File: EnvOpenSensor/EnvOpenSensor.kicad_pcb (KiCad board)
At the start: 2 copper layers, 89.7 x 67.5 mm, 31 parts, among them J1 USB_C_Receptacle_USB2.0_16P, J2 AVR-ISP-6, SW1 SW_Push, SW2 SW_Push, SW3 SW_Push, SW4 SW_Push, U1 SCD41-D-R2, U2 Si7021-A20, U3 SPX3819M5-L-3-3, U4 ATtiny85-20S

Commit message: forgot some stuff
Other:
- board text added: "EnvOpenSensor"
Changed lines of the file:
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@@
   )
   (footprint "Button_Switch_Keyboard:SW_Cherry_MX_1.00u_PCB" (layer "F.Cu")
-    (at 71.94 36.12)
+    (at 71.94 36.11)
     (descr "Cherry MX keyswitch, 1.00u, PCB mount, http://cherryamericas.com/wp-content/uploads/2014/12/mx_cat.pdf")
     (tags "Cherry MX keyswitch 1.00u PCB")
@@
   )
   (footprint "Button_Switch_Keyboard:SW_Cherry_MX_1.00u_PCB" (layer "F.Cu")
-    (at 33.44 36.12)
+    (at 33.39 36.12)
     (descr "Cherry MX keyswitch, 1.00u, PCB mount, http://cherryamericas.com/wp-content/uploads/2014/12/mx_cat.pdf")
     (tags "Cherry MX keyswitch 1.00u PCB")
@@
   )
   (footprint "Button_Switch_Keyboard:SW_Cherry_MX_1.00u_PCB" (layer "F.Cu")
-    (at 52.69 36.12)
+    (at 52.64 36.12)
     (descr "Cherry MX keyswitch, 1.00u, PCB mount, http://cherryamericas.com/wp-content/uploads/2014/12/mx_cat.pdf")
     (tags "Cherry MX keyswitch 1.00u PCB")
@@
   (gr_line (start 15 77.5) (end 15 15)
     (stroke (width 0.1) (type default)) (layer "Edge.Cuts"))
+  (gr_text "EnvOpenSensor" (at 59.75 31.9) (layer "F.Cu")
+    (effects (font (size 0.8 0.8) (thickness 0.15) bold))
+  )
   (gr_text "env" (at 59.825 70) (layer "F.Mask")
     (effects (font (face "Dissolve Regular") (size 5 5) (thickness 0.15)))

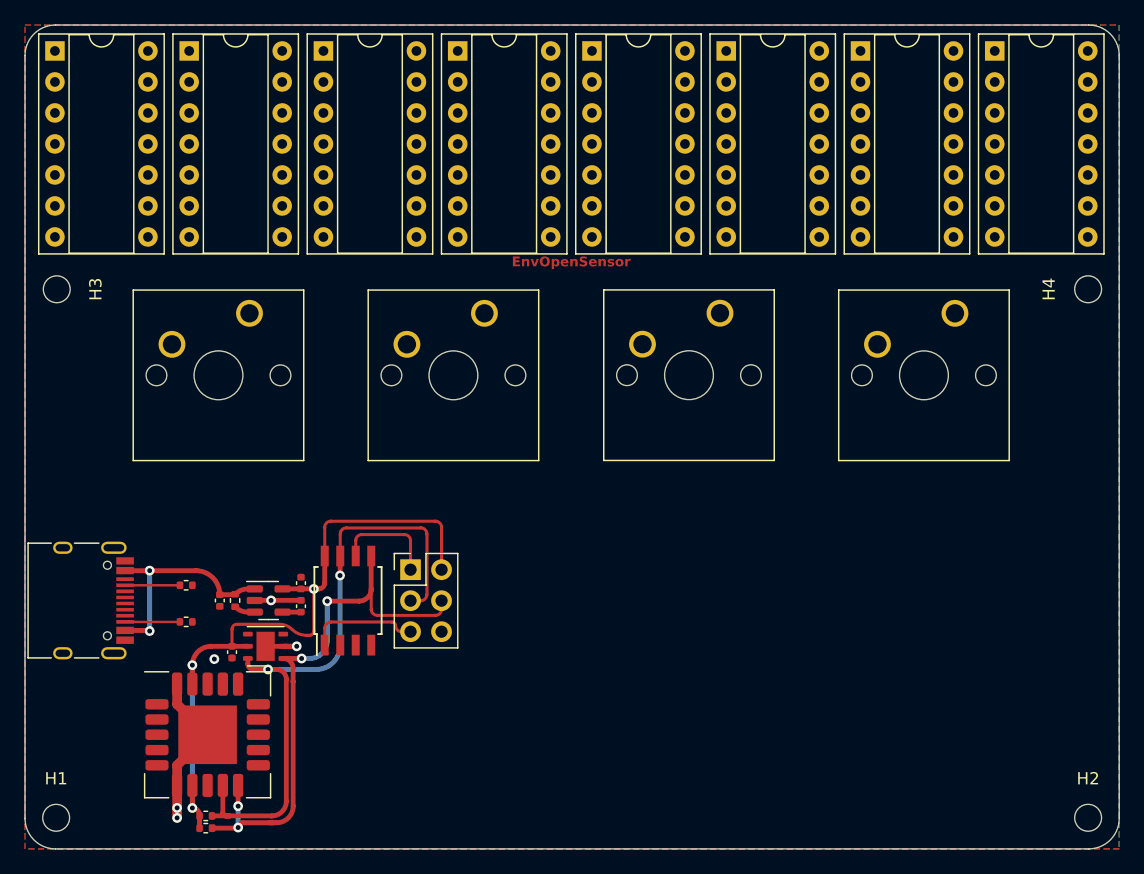
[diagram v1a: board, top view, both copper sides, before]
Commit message: added 3d models and shuffled some parts about for better usability.
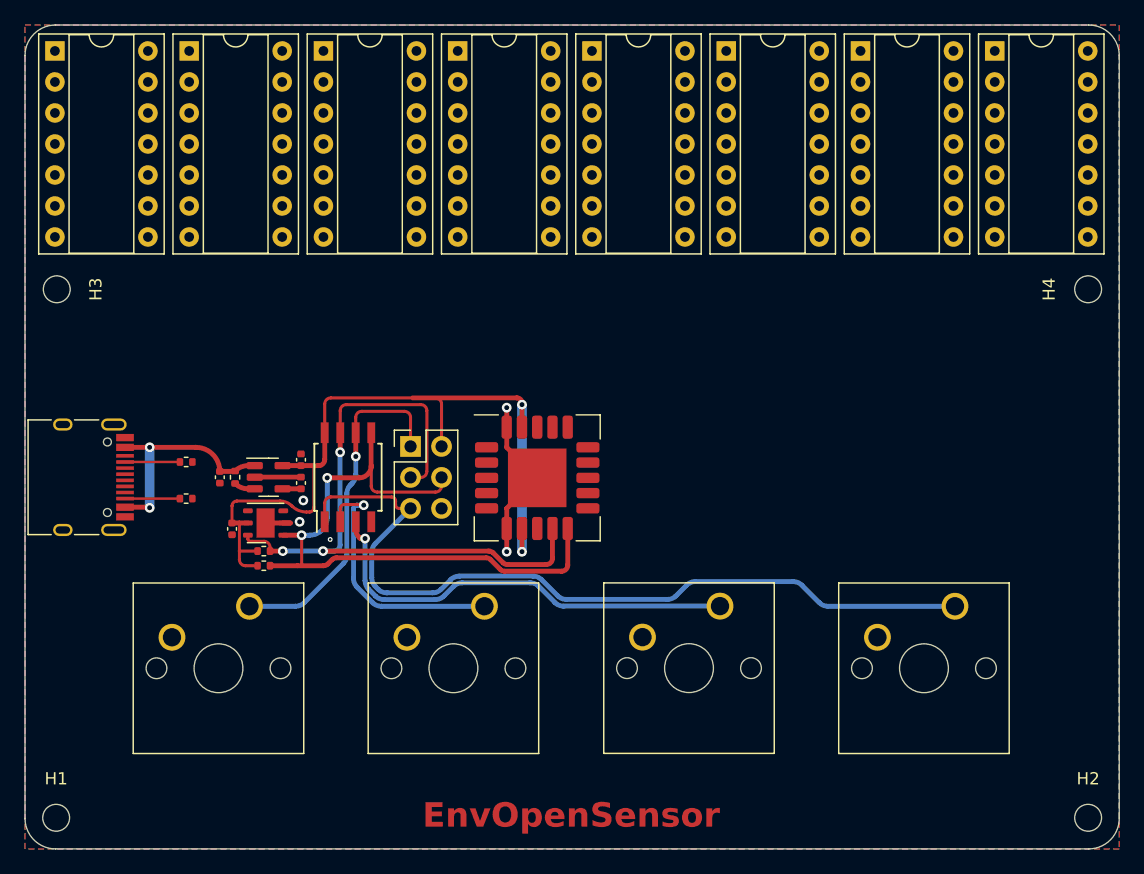
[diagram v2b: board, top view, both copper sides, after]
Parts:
- moved U1 34.2 mm to (57.0, 49.6)
- moved SW1 24.0 mm to (33.4, 60.1)
- moved SW2 24.0 mm to (52.6, 60.1)
- moved SW3 24.0 mm to (71.9, 60.1)
- moved SW4 24.0 mm to (91.2, 60.1)
- moved R5 22.2 mm to (34.6, 55.6)
- moved R4 22.0 mm to (34.6, 56.8)
- moved C2 10.1 mm to (31.0, 49.5)
- moved C3 10.1 mm to (37.6, 48.1)
- moved C4 10.1 mm to (32.0, 53.8)
- moved J1 10.1 mm to (19.1, 49.5)
- moved J2 10.1 mm to (46.6, 47.0)
- moved R1 10.1 mm to (28.2, 48.3)
- moved R2 10.1 mm to (28.2, 51.3)
- moved R3 10.1 mm to (32.2, 49.5)
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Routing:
- net PB5: track 9.10 -> 67.3 mm
- net PB4: track 0.00 -> 36.4 mm, vias 0 -> 1
- net PB3: track 0.00 -> 22.3 mm, vias 0 -> 1
- net PB1: track 8.65 -> 28.7 mm, vias 0 -> 1
- net +3V3: track 56.5 -> 66.7 mm, vias 3 -> 2
- net PB0: track 49.8 -> 57.1 mm, vias 4 -> 2
- net PB2: track 54.2 -> 55.9 mm, vias 2 -> 3
